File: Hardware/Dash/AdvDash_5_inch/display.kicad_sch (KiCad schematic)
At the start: 23 parts, among them J1 1-1734839-0, J2 54104-4031, Q2 AO3401A, Q3 S8050, U3 MT9201

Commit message: PCB R0.1.0
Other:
- company: (none) -> ADV.ECU - GNVPerformance
- title: (none) -> Display and Tocuh Panel main Connector

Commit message: :adhesive_bandage: Minor change to the PCB
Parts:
- C15, C17: LCSC (none) -> C602037
- C16, C20: LCSC (none) -> C28323
- C18, C19, C21, C23: LCSC (none) -> C38141
- C22: LCSC (none) -> C15850
- D7: LCSC (none) -> C35501
- J1: LCSC (none) -> C590935
- J2: LCSC (none) -> C164172
- L2: LCSC (none) -> C167253
- Q2: LCSC (none) -> C15127
- Q3: LCSC (none) -> C266592
- R15: LCSC (none) -> C25278
- R16: LCSC (none) -> C149504
- R17: value 10k -> 10K; LCSC (none) -> C17414
- R18: LCSC (none) -> C17408
- R19, R20: LCSC (none) -> C17673
- R21: LCSC (none) -> C17477
- U3: LCSC (none) -> C182966
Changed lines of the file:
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@@
+      (effects (font (size 1.27 1.27)) hide)
+    )
+    (property "LCSC" "C149504" (at 109.855 124.968 0)
       (effects (font (size 1.27 1.27)) hide)
     )
@@
       (effects (font (size 1.27 1.27)) (justify left) hide)
     )
+    (property "LCSC" "C266592" (at 101.6 128.778 0)
+      (effects (font (size 1.27 1.27)) hide)
+    )
     (pin "1")
     (pin "2")
@@
       (effects (font (size 1.27 1.27)) hide)
     )
+    (property "LCSC" "C35501" (at 191.77 126.238 0)
+      (effects (font (size 1.27 1.27)) hide)
+    )
     (pin "1")
     (pin "2")
@@
       (effects (font (size 1.27 1.27)) hide)
     )
+    (property "LCSC" "C602037" (at 207.645 130.048 0)
+      (effects (font (size 1.27 1.27)) hide)
+    )
     (pin "1")
     (pin "2")
@@
       (effects (font (size 1.27 1.27)) hide)
     )
+    (property "LCSC" "C38141" (at 246.38 75.565 0)
+      (effects (font (size 1.27 1.27)) hide)
+    )
     (pin "1")
     (pin "2")
@@
       (effects (font (size 1.27 1.27)) hide)
     )
+    (property "LCSC" "C28323" (at 147.32 130.048 0)
+      (effects (font (size 1.27 1.27)) hide)
+    )
     (pin "1")
     (pin "2")
@@
     (property "Manufacturer_Part_Number" "54104-4031" (at 214.63 824.765 0)
       (effects (font (size 1.27 1.27)) (justify left top) hide)
+    )
+    (property "LCSC" "C164172" (at 195.58 29.845 0)
+      (effects (font (size 1.27 1.27)) hide)
     )
     (pin "1")
@@
       (effects (font (size 1.27 1.27)) (justify left) hide)
     )
+    (property "LCSC" "C15127" (at 118.745 131.318 0)
+      (effects (font (size 1.27 1.27)) hide)
+    )
     (pin "1")
     (pin "2")
@@
       (effects (font (size 1.27 1.27)) hide)
     )
+    (property "LCSC" "C17673" (at 97.155 45.72 0)
+      (effects (font (size 1.27 1.27)) hide)
+    )
     (pin "1")
     (pin "2")
@@
       (effects (font (size 1.27 1.27)) hide)
     )
+    (property "LCSC" "C15850" (at 165.1 40.005 0)
+      (effects (font (size 1.27 1.27)) hide)
+    )
     (pin "1")
     (pin "2")
@@
     )
     (property "Datasheet" "" (at 168.91 127.508 0)
+      (effects (font (size 1.27 1.27)) hide)
+    )
+    (property "LCSC" "C182966" (at 168.91 127.508 0)
       (effects (font (size 1.27 1.27)) hide)
     )
@@
       (effects (font (size 1.27 1.27)) hide)
     )
+    (property "LCSC" "C602037" (at 138.43 130.048 0)
+      (effects (font (size 1.27 1.27)) hide)
+    )
     (pin "1")
     (pin "2")
@@
       (effects (font (size 1.27 1.27)) (justify left))
     )
-    (property "Value" "10k" (at 87.63 129.413 0)
+    (property "Value" "10K" (at 87.63 129.413 0)
       (effects (font (size 1.27 1.27)) (justify left))
     )
@@
       (effects (font (size 1.27 1.27)) hide)
     )
+    (property "LCSC" "C17414" (at 92.71 127.508 0)
+      (effects (font (size 1.27 1.27)) hide)
+    )
     (pin "1")
     (pin "2")
@@
       (effects (font (size 1.27 1.27)) hide)
     )
+    (property "LCSC" "C17408" (at 82.55 123.698 0)
+      (effects (font (size 1.27 1.27)) hide)
+    )
     (pin "1")
     (pin "2")
@@
     )
     (property "Datasheet" "~" (at 216.535 130.048 0)
+      (effects (font (size 1.27 1.27)) hide)
+    )
+    (property "LCSC" "C38141" (at 216.535 130.048 0)
       (effects (font (size 1.27 1.27)) hide)
     )
@@
       (effects (font (size 1.27 1.27)) hide)
     )
+    (property "LCSC" "C38141" (at 180.34 59.055 0)
+      (effects (font (size 1.27 1.27)) hide)
+    )
     (pin "1")
     (pin "2")
@@
       (effects (font (size 1.27 1.27)) hide)
     )
+    (property "LCSC" "C38141" (at 173.99 40.005 0)
+      (effects (font (size 1.27 1.27)) hide)
+    )
     (pin "1")
     (pin "2")
@@
       (effects (font (size 1.27 1.27)) hide)
     )
+    (property "LCSC" "C28323" (at 255.27 75.565 0)
+      (effects (font (size 1.27 1.27)) hide)
+    )
     (pin "1")
     (pin "2")
@@
       (effects (font (size 1.27 1.27)) hide)
     )
+    (property "LCSC" "C25278" (at 197.485 135.128 0)
+      (effects (font (size 1.27 1.27)) hide)
+    )
     (pin "1")
     (pin "2")
@@
       (effects (font (size 1.27 1.27)) hide)
     )
+    (property "LCSC" "C167253" (at 172.72 117.983 0)
+      (effects (font (size 1.27 1.27)) hide)
+    )
     (pin "1")
     (pin "2")
@@
       (effects (font (size 1.27 1.27)) hide)
     )
+    (property "LCSC" "C17673" (at 93.345 45.72 0)
+      (effects (font (size 1.27 1.27)) hide)
+    )
     (pin "1")
     (pin "2")
@@
     (property "Manufacturer_Part_Number" "1-1734839-0" (at 69.85 841.91 0)
       (effects (font (size 1.27 1.27)) (justify left top) hide)
+    )
+    (property "LCSC" "C590935" (at 48.26 46.99 0)
+      (effects (font (size 1.27 1.27)) hide)
     )
     (pin "1")
@@
       (effects (font (size 1.27 1.27)) hide)
     )
+    (property "LCSC" "C17477" (at 169.545 55.245 0)
+      (effects (font (size 1.27 1.27)) hide)
+    )

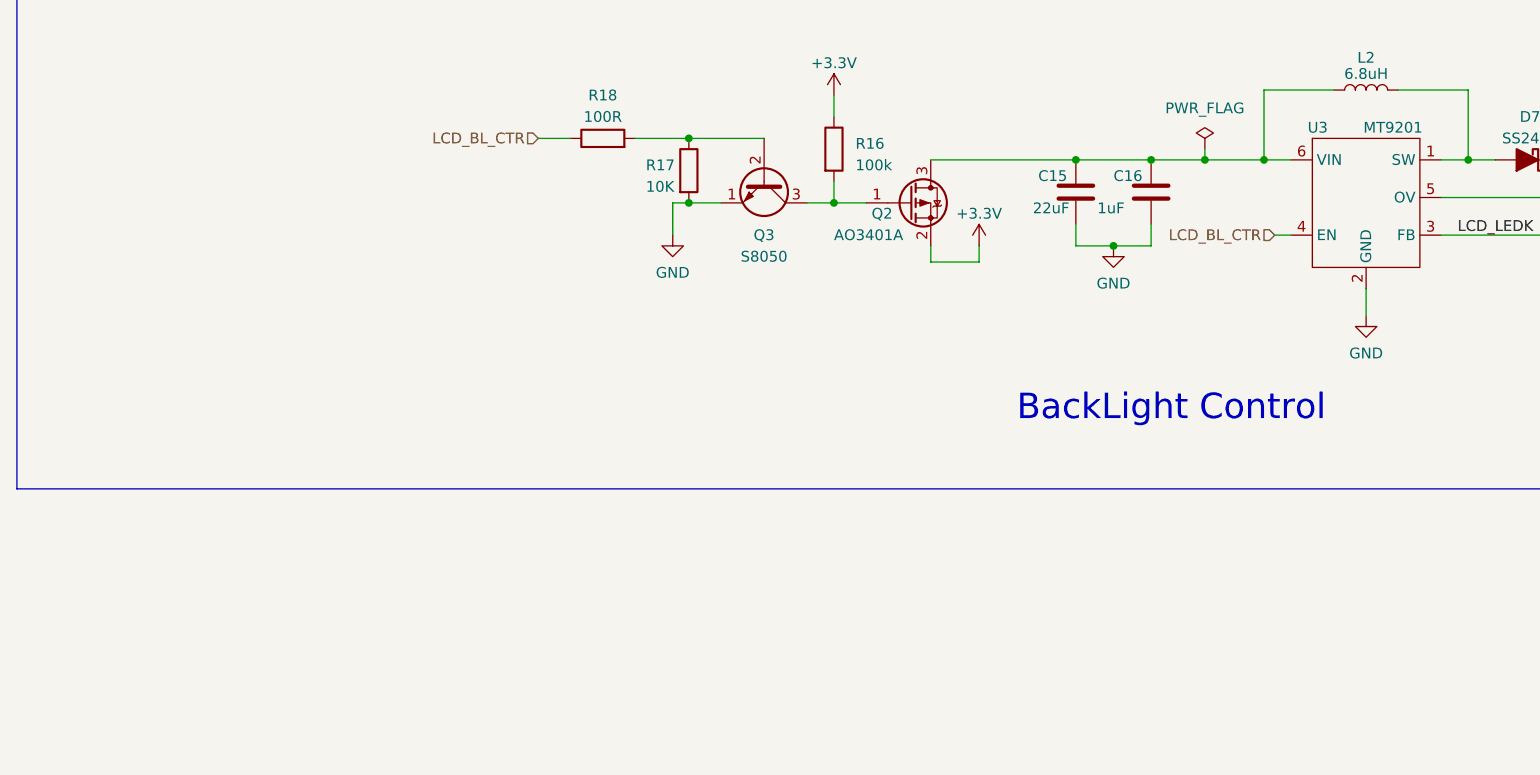
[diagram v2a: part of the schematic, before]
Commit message: :adhesive_bandage: Fix errors in pcb desing, changelog in file, rev0.2.0
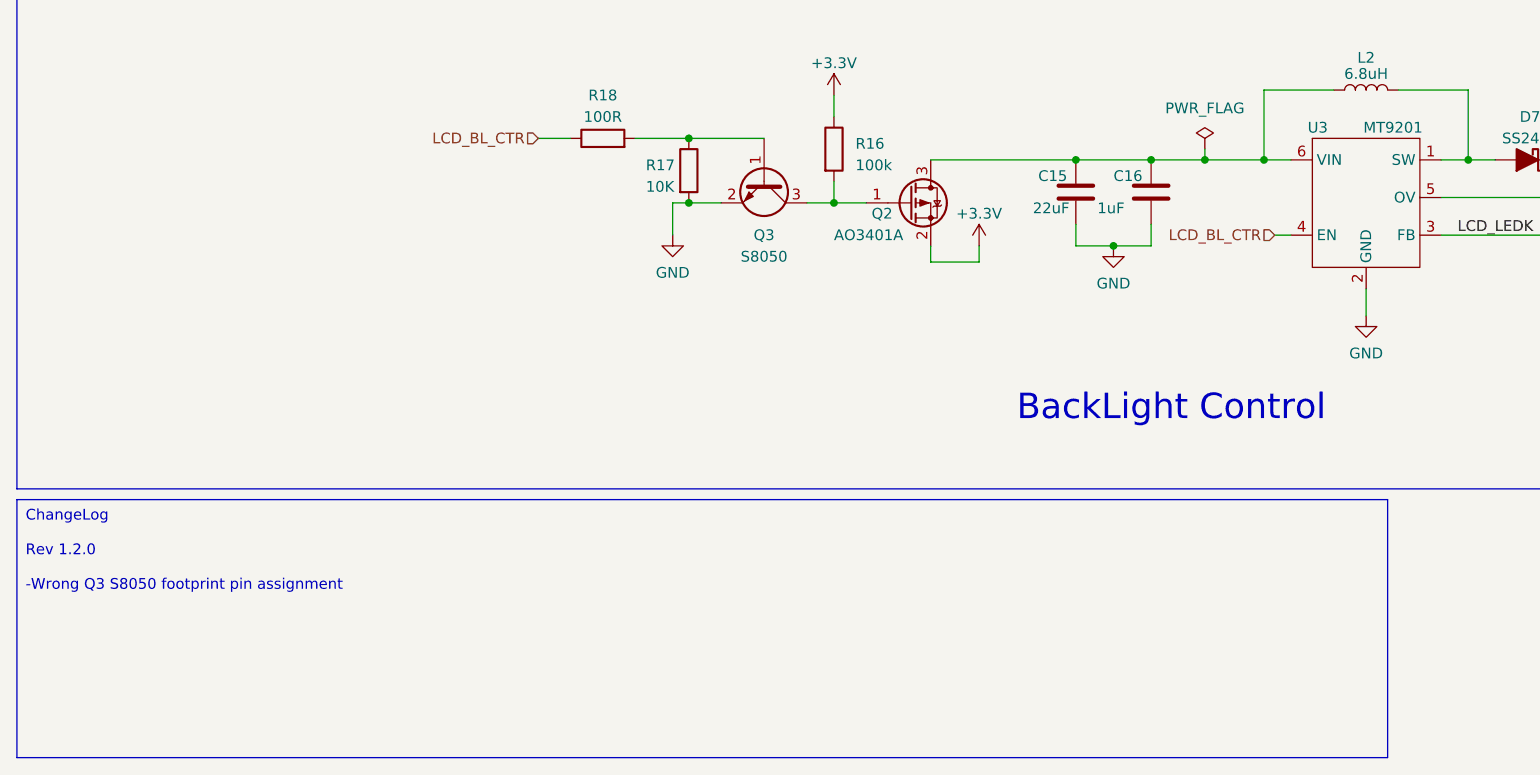
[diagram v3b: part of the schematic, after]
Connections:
- net GND: now also Q3.2 (E); no longer Q3.1 (E)
- net at R17.1, R18.2: now also Q3.1 (B); no longer Q3.2 (B)
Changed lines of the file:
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@@
     (title "Display and Tocuh Panel main Connector")
     (date "2023-10-27")
-    (rev "0.1.0")
+    (rev "0.2.0")
     (company "ADV.ECU - GNVPerformance")
   )
@@
     )
   )
+  (text_box "ChangeLog\n\nRev 1.2.0\n\n-Wrong Q3 S8050 footprint pin assignment"
+    (at 13.335 166.37 0) (size 161.925 30.48)
+    (stroke (width 0) (type default))
+    (fill (type none))
+    (effects (font (size 1.27 1.27)) (justify left top))
+  )
   (text "LCD Connector" (at 191.77 99.695 0)
     (effects (font (size 3 3)) (justify left bottom))
@@
       (effects (font (size 1.27 1.27)) hide)
     )
+    (property "MOUSER" "" (at 101.6 128.778 0)
+      (effects (font (size 1.27 1.27)))
+    )
+    (pin "2")
     (pin "1")
-    (pin "2")
     (pin "3")
     (instances

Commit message: :bug: PCB R0.2.0 Ready, change log in kicad files
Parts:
- added JP4: Reset Control, Jumper:SolderJumper-3_P1.3mm_Open_Pad1.0x1.5mm, symbol Jumper:SolderJumper_3_Open
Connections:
- net TP_RST: now also JP4.1 (A); no longer J1.7
- new net: J1.7, JP4.2 (C)
- new net TP_RST_2: JP4.3 (B)
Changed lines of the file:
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@@
   (no_connect (at 73.66 67.31))
   (no_connect (at 195.58 42.545))
-  (wire (pts (xy 73.66 62.23) (xy 76.2 62.23))
-    (stroke (width 0) (type default))
-  )
   (wire (pts (xy 127 136.398) (xy 127 138.303))
     (stroke (width 0) (type default))
@@
     (stroke (width 0) (type default))
   )
+  (wire (pts (xy 99.695 74.295) (xy 106.045 74.295))
+    (stroke (width 0) (type default))
+  )
   (wire (pts (xy 195.58 75.565) (xy 184.785 75.565))
     (stroke (width 0) (type default))
@@
     (stroke (width 0) (type default))
   )
+  (wire (pts (xy 99.695 60.96) (xy 106.68 60.96))
+    (stroke (width 0) (type default))
+  )
   (wire (pts (xy 93.345 52.07) (xy 98.425 52.07))
     (stroke (width 0) (type default))
@@
     (stroke (width 0) (type default))
   )
+  (wire (pts (xy 99.695 74.295) (xy 99.695 72.39))
+    (stroke (width 0) (type default))
+  )
   (wire (pts (xy 173.355 55.245) (xy 180.34 55.245))
     (stroke (width 0) (type default))
@@
     (stroke (width 0) (type default))
   )
+  (wire (pts (xy 95.885 67.31) (xy 93.345 67.31))
+    (stroke (width 0) (type default))
+  )
   (wire (pts (xy 109.855 131.318) (xy 113.665 131.318))
     (stroke (width 0) (type default))
@@
     (stroke (width 0) (type default))
   )
+  (wire (pts (xy 93.345 67.31) (xy 93.345 62.23))
+    (stroke (width 0) (type default))
+  )
   (wire (pts (xy 180.34 62.865) (xy 180.34 73.025))
     (stroke (width 0) (type default))
@@
     (stroke (width 0) (type default))
   )
+  (wire (pts (xy 99.695 60.96) (xy 99.695 62.23))
+    (stroke (width 0) (type default))
+  )
   (wire (pts (xy 73.66 54.61) (xy 86.995 54.61))
     (stroke (width 0) (type default))
@@
   )
   (wire (pts (xy 190.5 67.945) (xy 195.58 67.945))
+    (stroke (width 0) (type default))
+  )
+  (wire (pts (xy 73.66 62.23) (xy 93.345 62.23))
     (stroke (width 0) (type default))
   )
@@
     )
   )
-  (text_box "ChangeLog\n\nRev 1.2.0\n\n-Wrong Q3 S8050 footprint pin assignment"
+  (text_box "ChangeLog\n\nRev 1.2.0\n\n-Wrong Q3 S8050 footprint pin assignment\n\n-The reset of the tocuh caused that when going to spleep it started again, a jumper is set and an independent pin is assigned for control"
     (at 13.335 166.37 0) (size 161.925 30.48)
     (stroke (width 0) (type default))
@@
     (effects (font (size 1.27 1.27)) (justify right))
   )
-  (hierarchical_label "TP_RST" (shape input) (at 76.2 62.23 0) (fields_autoplaced)
+  (hierarchical_label "TP_RST" (shape input) (at 106.68 60.96 0) (fields_autoplaced)
     (effects (font (size 1.27 1.27)) (justify left))
   )
@@
     (effects (font (size 1.27 1.27)) (justify right))
   )
+  (hierarchical_label "TP_RST_2" (shape input) (at 106.045 74.295 0) (fields_autoplaced)
+    (effects (font (size 1.27 1.27)) (justify left))
+  )
   (hierarchical_label "B7" (shape input) (at 190.5 60.325 180) (fields_autoplaced)
     (effects (font (size 1.27 1.27)) (justify right))
@@
       (effects (font (size 1.27 1.27)))
     )
-    (pin "2")
-    (pin "1")
+    (pin "1")
+    (pin "2")
     (pin "3")
     (instances
@@
         )
       )
+    )
+  )
+  (symbol (lib_id "Jumper:SolderJumper_3_Open") (at 99.695 67.31 270) (unit 1)
+    (in_bom yes) (on_board yes) (dnp no)
+    (property "Reference" "JP4" (at 102.87 67.31 90)
+      (effects (font (size 1.27 1.27)))
+    )
+    (property "Value" "Reset Control" (at 107.315 69.215 90)
+      (effects (font (size 1.27 1.27)))
+    )
+    (property "Footprint" "Jumper:SolderJumper-3_P1.3mm_Open_Pad1.0x1.5mm" (at 99.695 67.31 0)
+      (effects (font (size 1.27 1.27)) hide)
+    )
+    (property "Datasheet" "~" (at 99.695 67.31 0)
+      (effects (font (size 1.27 1.27)) hide)
+    )
+    (pin "1")
+    (pin "2")
+    (pin "3")
+    (instances
+      (project "_autosave-ADVgauge_controller v1.0.0 - S3"
+        (path "/2e106c18-3d45-4af9-8365-7b264e2e9016"
+          (reference "JP4") (unit 1)
+        )
+      )
+      (project "AdvDash_5_inch"
+        (path "/dc9c4178-e1bb-4529-992c-1528c3a3fad9/194a57e8-5d7d-4fec-9e8a-841ca2e34ec8"
+          (reference "JP3") (unit 1)
+        )
+        (path "/dc9c4178-e1bb-4529-992c-1528c3a3fad9/e0d1b0d5-ac5d-4cb2-adbd-1bf1d724da78"
+          (reference "JP5") (unit 1)
+        )
+      )
